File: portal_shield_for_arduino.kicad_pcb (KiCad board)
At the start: 2 copper layers, 54.5 x 53.3 mm, 35 parts, among them J1 ATX_BTN_CONN, J2 CAMERA_CONFIG, J3 CAMERA_CONN, J4 LIGHT_CONFIG, J5 LIGHT_CONN, K1 Relay_Panasonic_PA1a_XX_DIP, P1 Power, P2 Analog, P3 Digital, P4 Digital, P5 CONN_01X01, P7 CONN_01X01, Q1 STP16NF06L, Q2 FDN340P, Q3 FDN340P, Q4 STP16NF06L, Q5 FDN340P, U1 LTV-817S, U2 LTV-817S, U3 LTV-817S

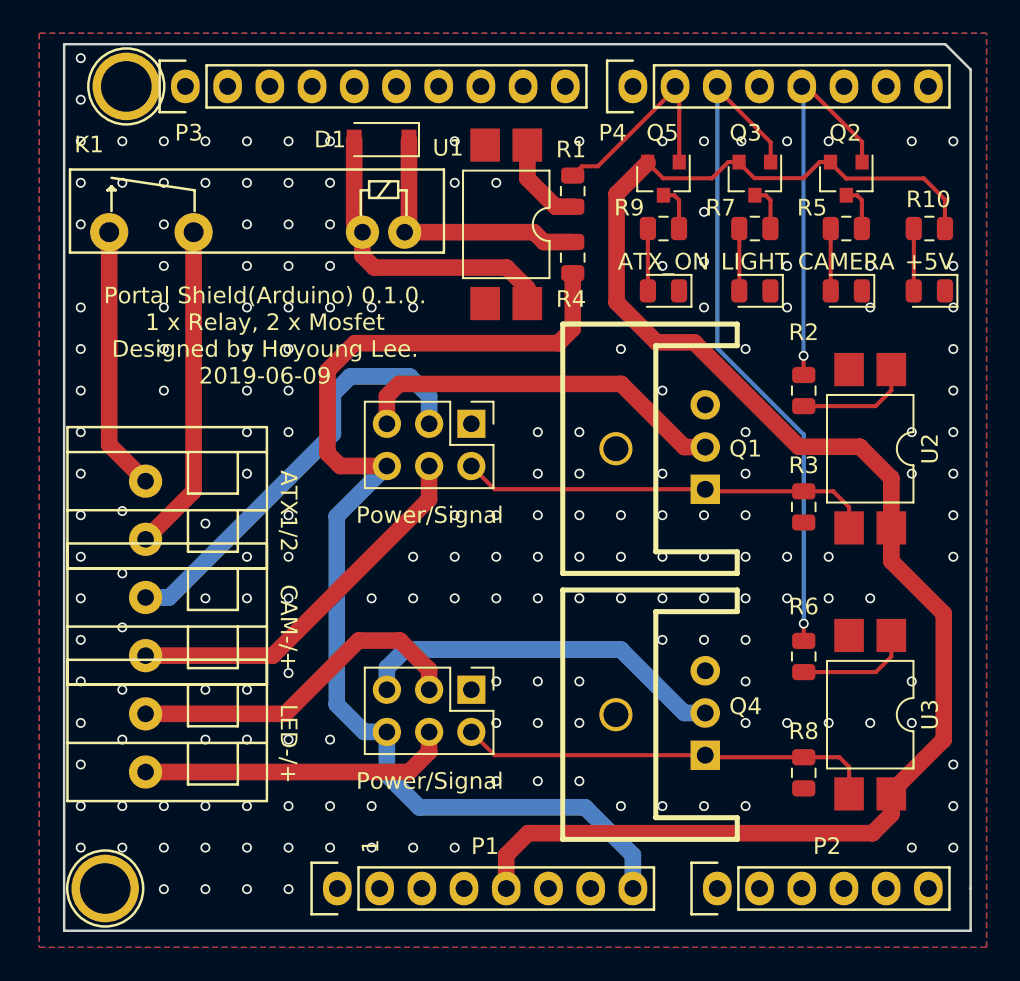
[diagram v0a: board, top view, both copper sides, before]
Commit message: modified to ease the connection of DSUB9, and add labels for terminals
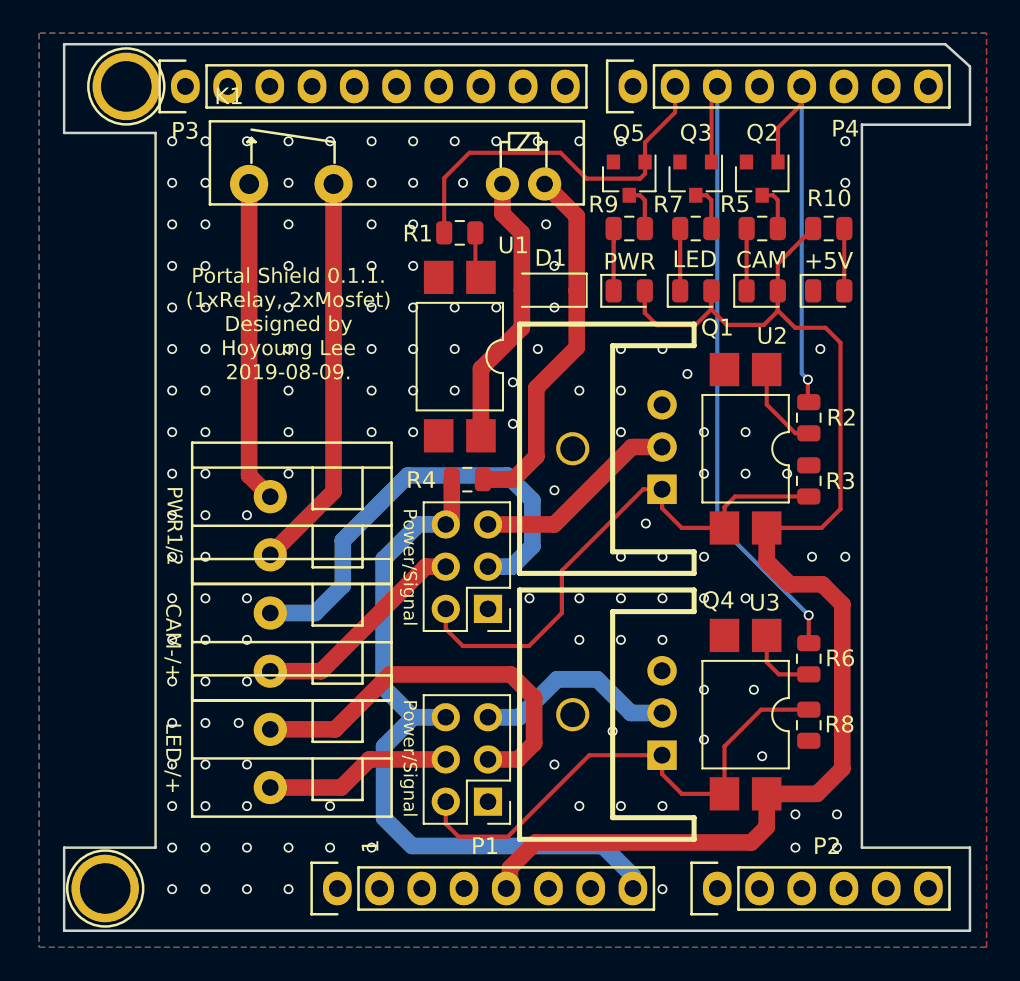
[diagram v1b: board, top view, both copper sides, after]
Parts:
- Q2, Q3, Q5: value FDN340P -> BSS123LT1
- moved R4 14.8 mm to (146.8, 99.2), turned to 0 degrees
- moved D1 13.6 mm to (151.7, 87.8)
- moved J2 11.2 mm to (148.0, 107.0), turned to 180 degrees
- moved K1 8.91 mm to (142.5, 80.2)
- moved U1 8.43 mm to (146.3, 91.8)
- moved J1 7.56 mm to (136.2, 102.0)
- moved J3 7.56 mm to (136.2, 109.0)
- moved J5 7.56 mm to (136.2, 116.0)
- moved U2 7.50 mm to (163.5, 97.4)
- moved U3 7.50 mm to (163.5, 113.4)
- moved R1 7.24 mm to (146.3, 84.4), turned to 180 degrees
- moved J4 6.81 mm to (148.0, 118.6), turned to 180 degrees
- moved +5V 6.06 mm to (168.5, 87.9), turned to 0 degrees
- moved R10 6.06 mm to (168.5, 84.1), turned to 0 degrees
- moved CAM 5.06 mm to (164.5, 87.9), turned to 0 degrees
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- renumbered CAMERA to CAM, LIGHT to LED, ATX_ON to PWR
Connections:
- CAM pad 1: GND -> Net-(D2-Pad1)
- CAM pad 2: Net-(D2-Pad2) -> +5V
- LED pad 1: GND -> Net-(D3-Pad1)
- LED pad 2: Net-(D3-Pad2) -> +5V
- PWR pad 1: GND -> Net-(D4-Pad1)
- PWR pad 2: Net-(D4-Pad2) -> +5V
- Q2 pad 2: +5V -> GND
- Q3 pad 2: +5V -> GND
- Q5 pad 2: +5V -> GND
- R5 pad 1: Net-(D2-Pad2) -> Net-(Q2-Pad3)
- R5 pad 2: Net-(Q2-Pad3) -> Net-(D2-Pad1)
- R7 pad 1: Net-(Q3-Pad3) -> Net-(D3-Pad1)
- R7 pad 2: Net-(D3-Pad2) -> Net-(Q3-Pad3)
- R9 pad 1: Net-(Q5-Pad3) -> Net-(D4-Pad1)
- R9 pad 2: Net-(D4-Pad2) -> Net-(Q5-Pad3)
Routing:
- net /Vin(12V): track 68.7 -> 43.6 mm
- net +5V: track 101.5 -> 82.0 mm
- net Net-(J2-Pad5): track 22.7 -> 12.4 mm
- net Net-(J4-Pad5): track 22.5 -> 12.3 mm
- net Net-(J2-Pad4): track 23.0 -> 13.2 mm
- net /6(**): track 13.1 -> 22.8 mm
- net Net-(J4-Pad4): track 18.8 -> 11.3 mm
- net Net-(J2-Pad2): track 25.1 -> 32.0 mm
- net Net-(D1-Pad1): track 16.0 -> 22.0 mm
- net Net-(J4-Pad2): track 25.2 -> 30.9 mm
- net Net-(J1-Pad1): track 19.7 -> 23.9 mm
- net Net-(D4-Pad2): track 3.75 -> 0.00 mm
- net Net-(D4-Pad1): track 0.00 -> 3.75 mm
- net Net-(D3-Pad2): track 3.75 -> 0.00 mm
- net Net-(D3-Pad1): track 0.00 -> 3.75 mm
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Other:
- outline, holes or cut-outs redrawn
- board text added: "PWR1/2"
- board text added: "Portal Shield 0.1.1. (1xRelay, 2xMosfet) Designed by Hoyoung Lee 2019-08-09."
- board text removed: "ATX1/2"
- board text removed: "Portal Shield(Arduino) 0.1.0. 1 x Relay, 2 x Mosfet Designed by Hoyoung Lee. 2019-06-09"
